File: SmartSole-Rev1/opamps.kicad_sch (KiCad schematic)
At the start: 22 parts, among them U1 MCP6004

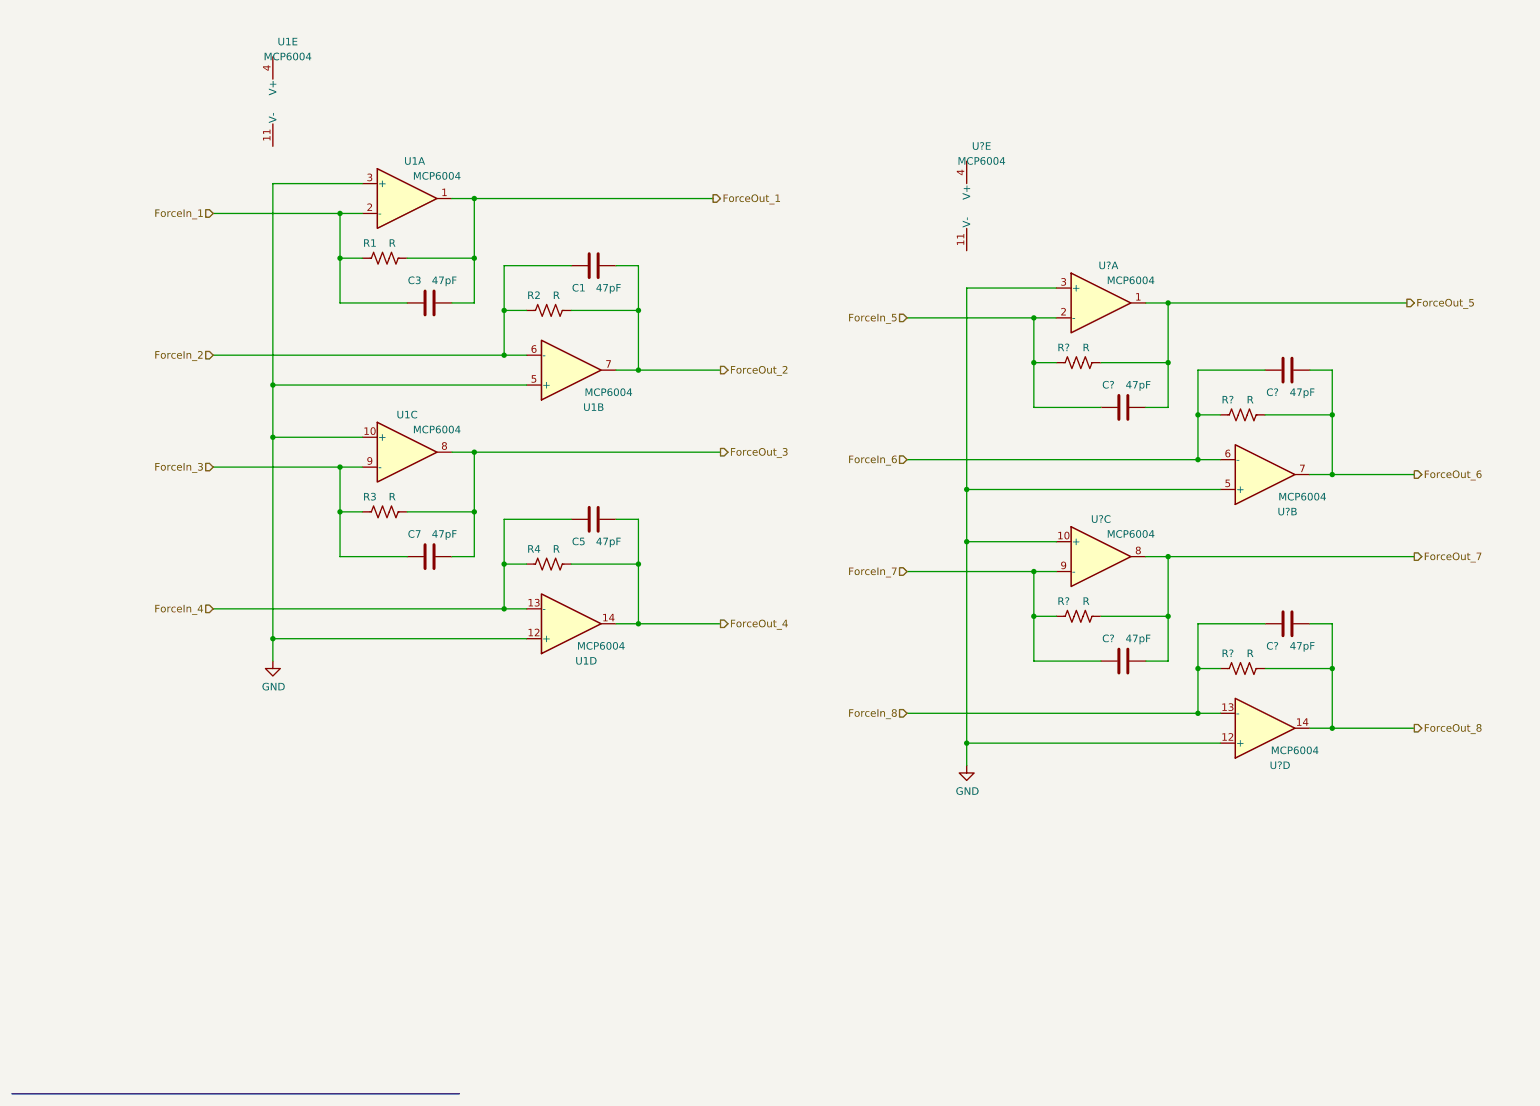
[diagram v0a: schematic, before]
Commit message: Created draft reference voltage circuit for force sensors
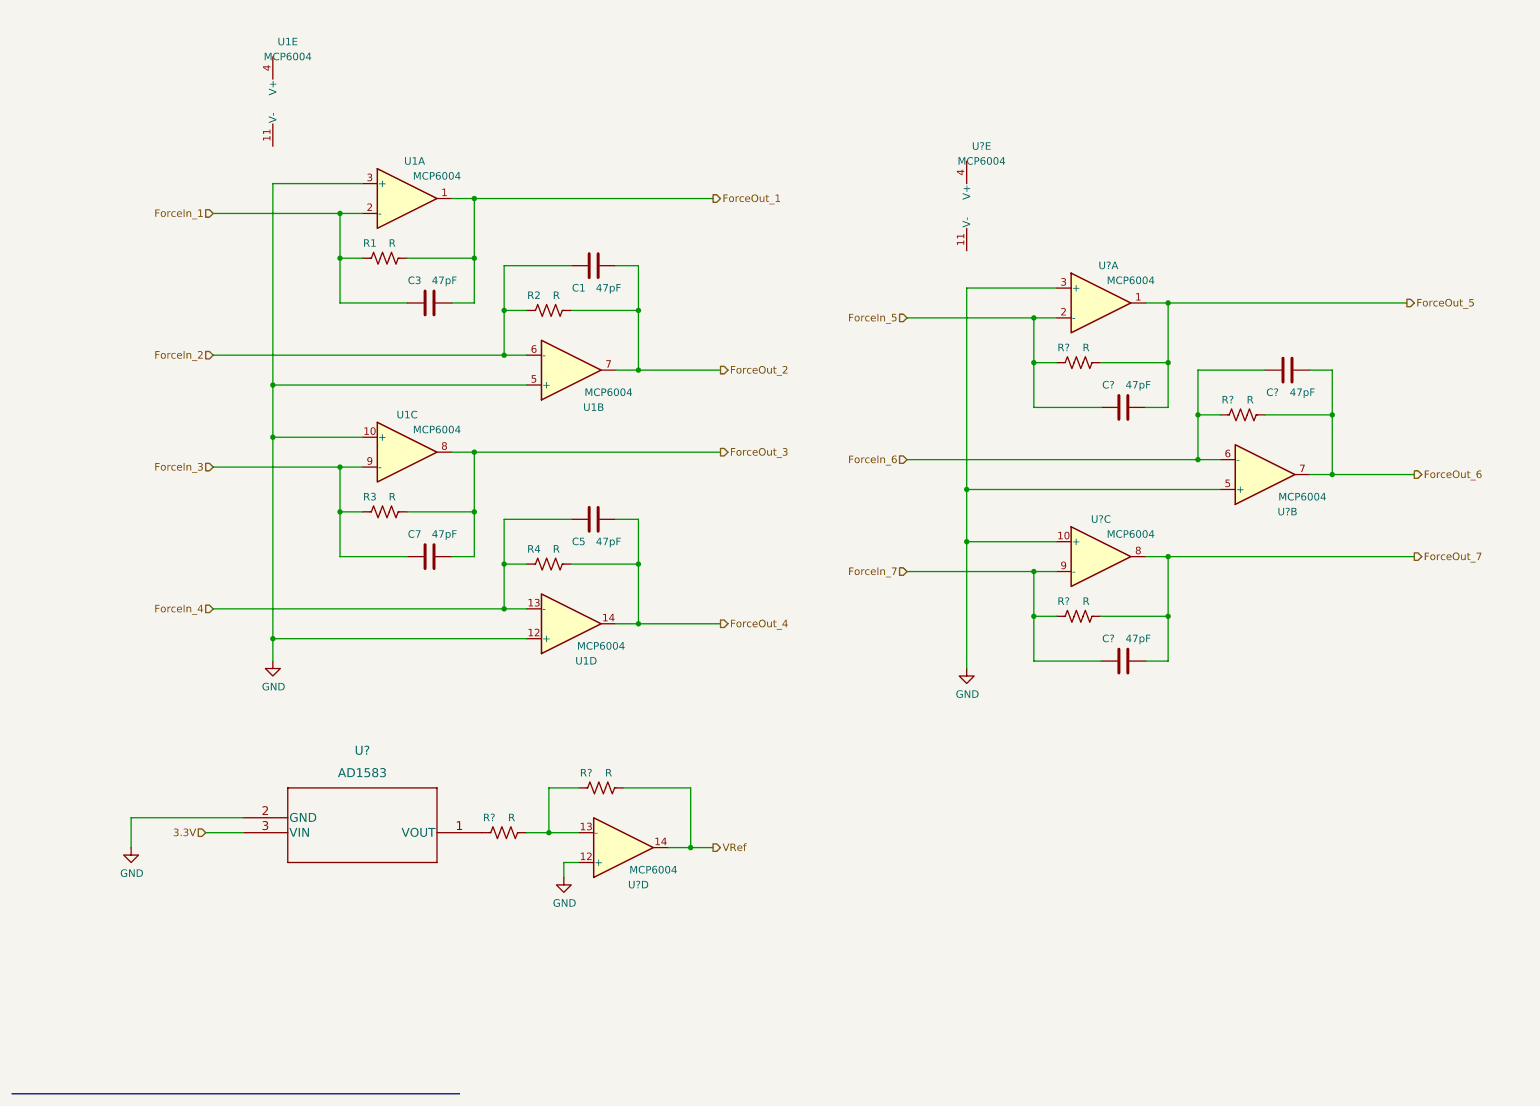
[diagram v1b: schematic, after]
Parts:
- removed C?: 47pF, Capacitor_SMD:C_0603_1608Metric, symbol Device:C
- removed R?: R, Resistor_SMD:R_0603_1608Metric, symbol Device:R_US
- added R? (x2): R, Resistor_SMD:R_0603_1608Metric, symbol Device:R_US
- added U?: AD1583, CapstoneLibrary:AD1583ARTZ-Reel7, symbol CapstoneLibrary:AD1583
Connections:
- net GND: now also U?.2 (GND)
- net ForceIn_8: no longer names the net of U?.13 (-)
- net ForceIn_8: now also R?.1, R?.2
- net ForceOut_8 renamed VRef
- net VRef: now also R?.2
- new net: R?.1, U?.1 (VOUT)
- new net 3.3V: U?.3 (VIN)
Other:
- moved on the sheet: U?D

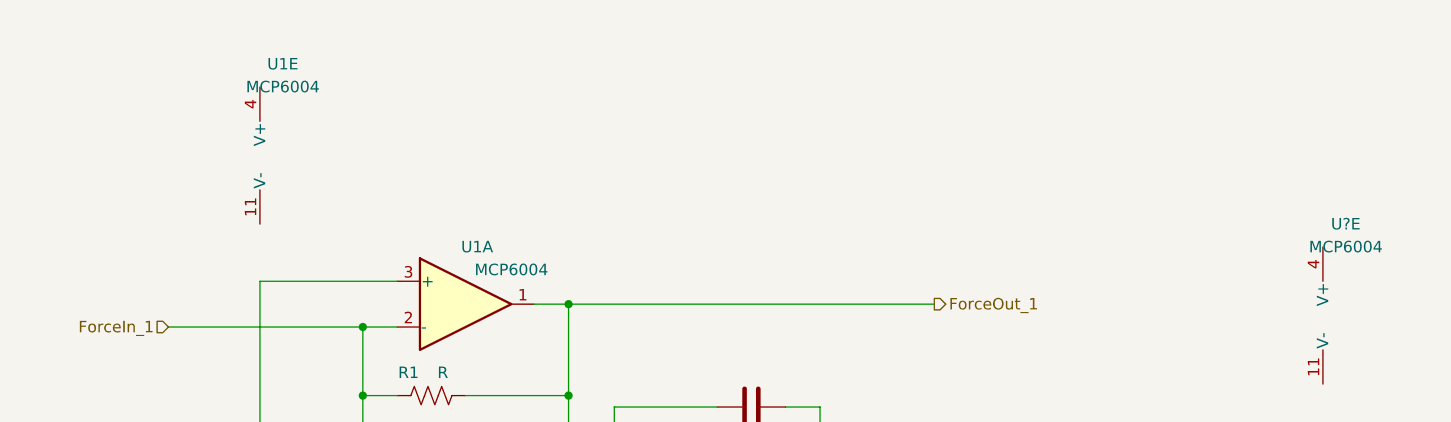
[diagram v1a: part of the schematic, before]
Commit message: Created model for header connectors to Sparkfun nrf mod
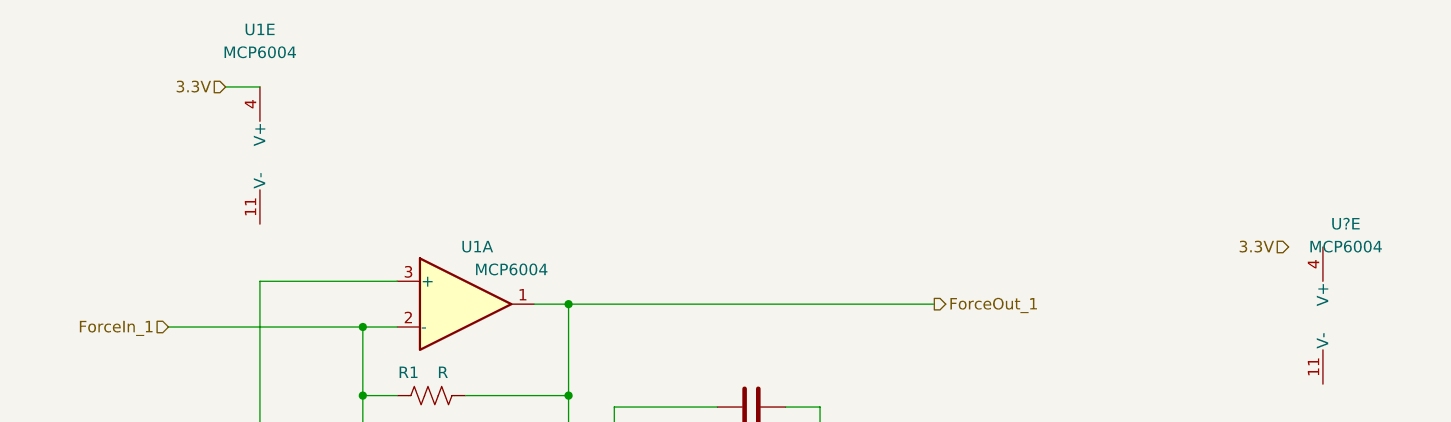
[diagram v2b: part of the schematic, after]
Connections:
- net 3.3V: now also U1.4 (V+)
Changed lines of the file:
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@@
+    (stroke (width 0) (type default) (color 0 0 0 0))
+  )
+  (wire (pts (xy 59.69 22.86) (xy 63.5 22.86))
     (stroke (width 0) (type default) (color 0 0 0 0))
   )
@@
   )
   (hierarchical_label "ForceIn_3" (shape input) (at 53.34 92.71 180)
+    (effects (font (size 1.27 1.27)) (justify right))
+  )
+  (hierarchical_label "3.3V" (shape input) (at 59.69 22.86 180)
+    (effects (font (size 1.27 1.27)) (justify right))
+  )
+  (hierarchical_label "3.3V" (shape input) (at 177.8 40.64 180)
     (effects (font (size 1.27 1.27)) (justify right))
   )
@@
   )
   (symbol (lib_id "Amplifier_Operational:MCP6004") (at 66.04 30.48 0) (unit 5)
-    (in_bom yes) (on_board yes) (fields_autoplaced)
-    (property "Reference" "U1" (id 0) (at 66.04 20.32 0))
-    (property "Value" "MCP6004" (id 1) (at 66.04 22.86 0))
+    (in_bom yes) (on_board yes)
+    (property "Reference" "U1" (id 0) (at 63.5 16.51 0))
+    (property "Value" "MCP6004" (id 1) (at 63.5 19.05 0))
     (property "Footprint" "Package_DIP:DIP-14_W7.62mm" (id 2) (at 64.77 27.94 0)
       (effects (font (size 1.27 1.27)) hide)
